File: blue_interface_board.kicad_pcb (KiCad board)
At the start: 4 copper layers, 70 x 70 mm, 123 parts, among them J1 arm connector, J2 USB_B_Micro, J3 ESTOP, J4 PWR, J5 Conn_ARM_JTAG_SWD_10, J6 logic-side RS485 debug/expans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, J7 FAN, J8 power-side RS485 debug/expans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, Q1 MMBT5401LT1G, Q2 Q_NMOS_GDS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

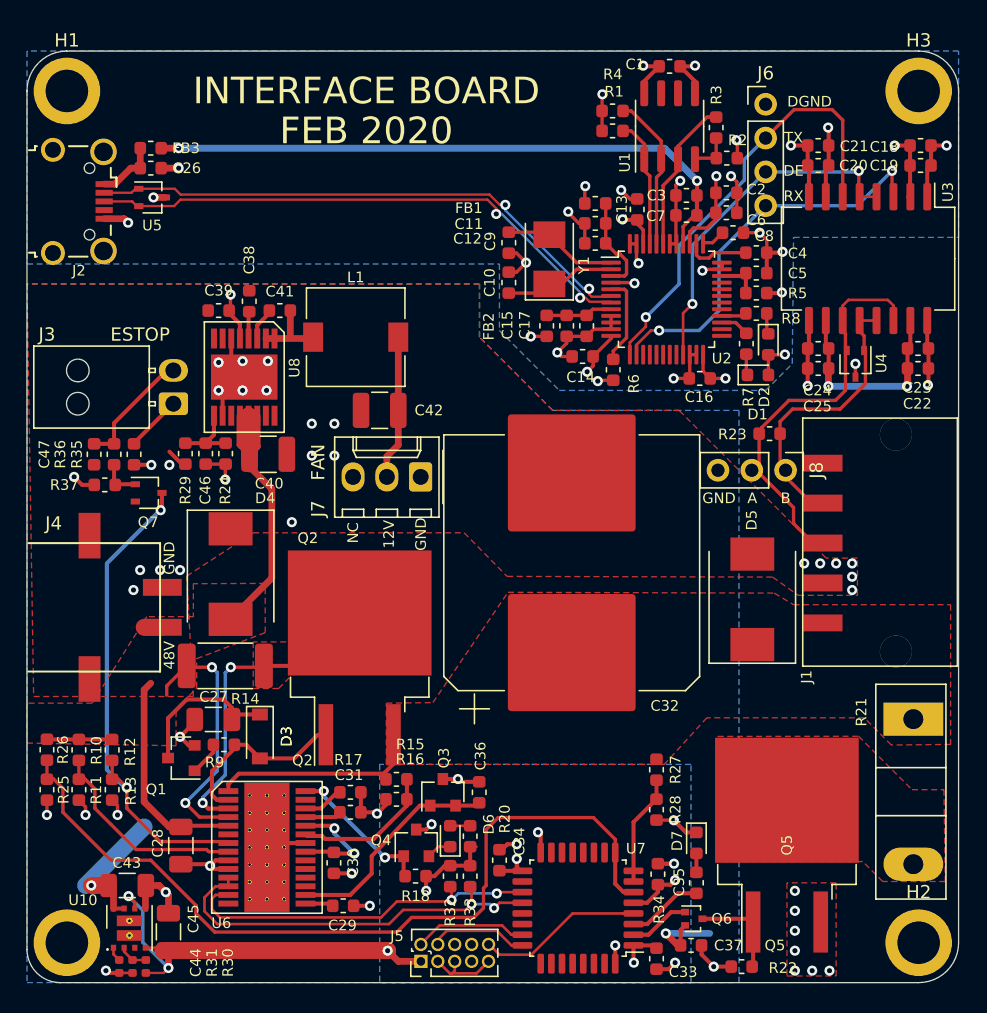
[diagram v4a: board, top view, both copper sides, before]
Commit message: recalculate lm5066 passives
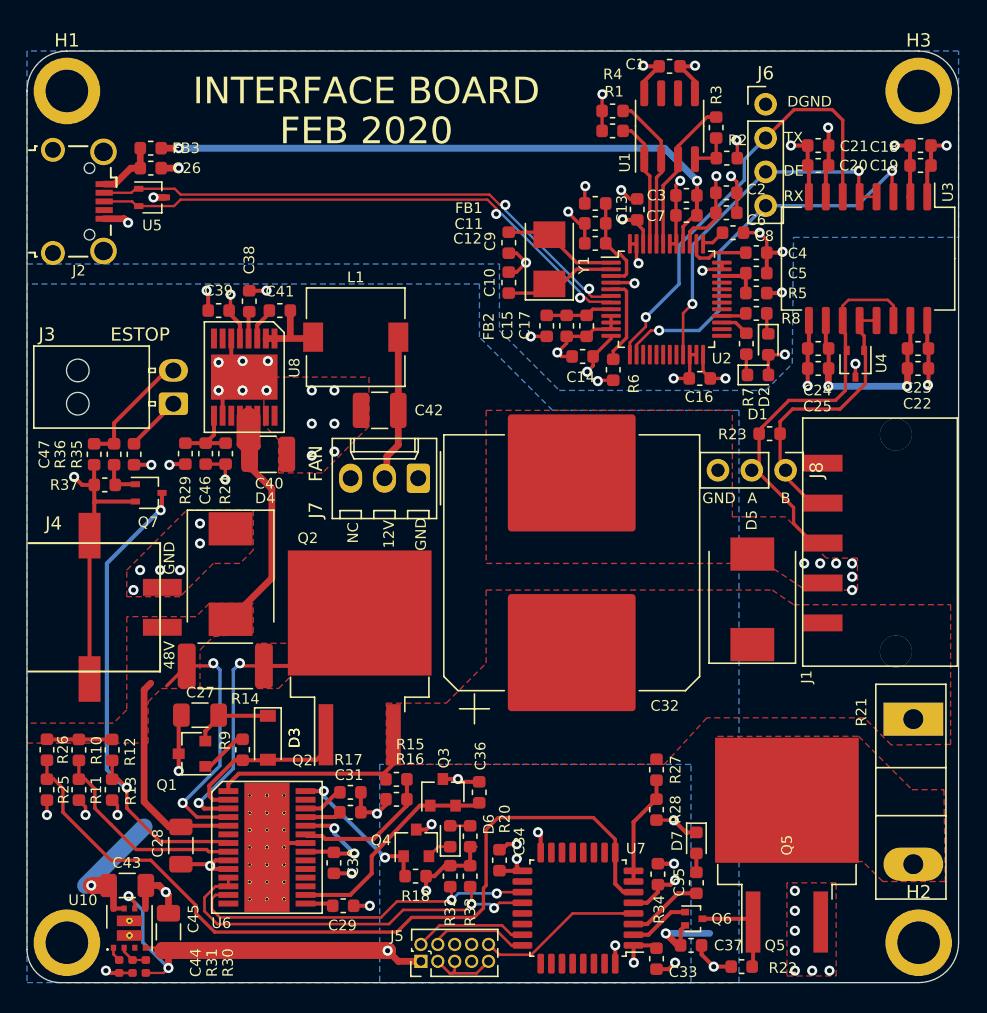
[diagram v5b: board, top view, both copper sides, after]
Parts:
- Q2: value Q_NMOS_GDS -> PSMN4R8-100BSEJ
- R11: value 6k65 -> 6k5
- R14: value 10m -> 15m
- R15: value 240k -> 140k
- R16: value 13.3k -> 21k
- R17: value 240k -> 21k
- moved R9 1.45 mm to (105.2, 111.5), turned to 90 degrees
- moved C27 1.05 mm to (102.0, 108.9)
- moved Q1 0.86 mm to (101.4, 111.8)
- moved D3 0.61 mm to (107.1, 110.6)
- moved J7 0.21 mm to (118.4, 91.1)
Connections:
- Q1 pad 2: GND -> Net-(C27-Pad1)
- Q1 pad 3: Net-(C27-Pad1) -> GND
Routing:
- net GND: track 73.3 -> 96.2 mm, vias 52 -> 57
- net Net-(C27-Pad1): track 11.8 -> 6.08 mm
- net /Power/VIN: track 66.7 -> 65.5 mm
- net Net-(Q1-Pad1): track 2.54 -> 3.64 mm

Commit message: fix Q3 pinout and chase a few part numbers
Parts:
- moved C36 0.63 mm to (122.3, 114.7), turned to -90 degrees
- moved Q3 0.45 mm to (119.8, 114.7)
- moved R15 0.36 mm to (116.4, 113.7)
- moved R16 0.36 mm to (116.4, 115.2)
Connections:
- Q3 pad 2: Net-(C36-Pad1) -> GND
- Q3 pad 3: GND -> Net-(C36-Pad1)
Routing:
- net Net-(R15-Pad1): track 11.1 -> 9.80 mm
- net Net-(C36-Pad1): track 16.7 -> 17.7 mm

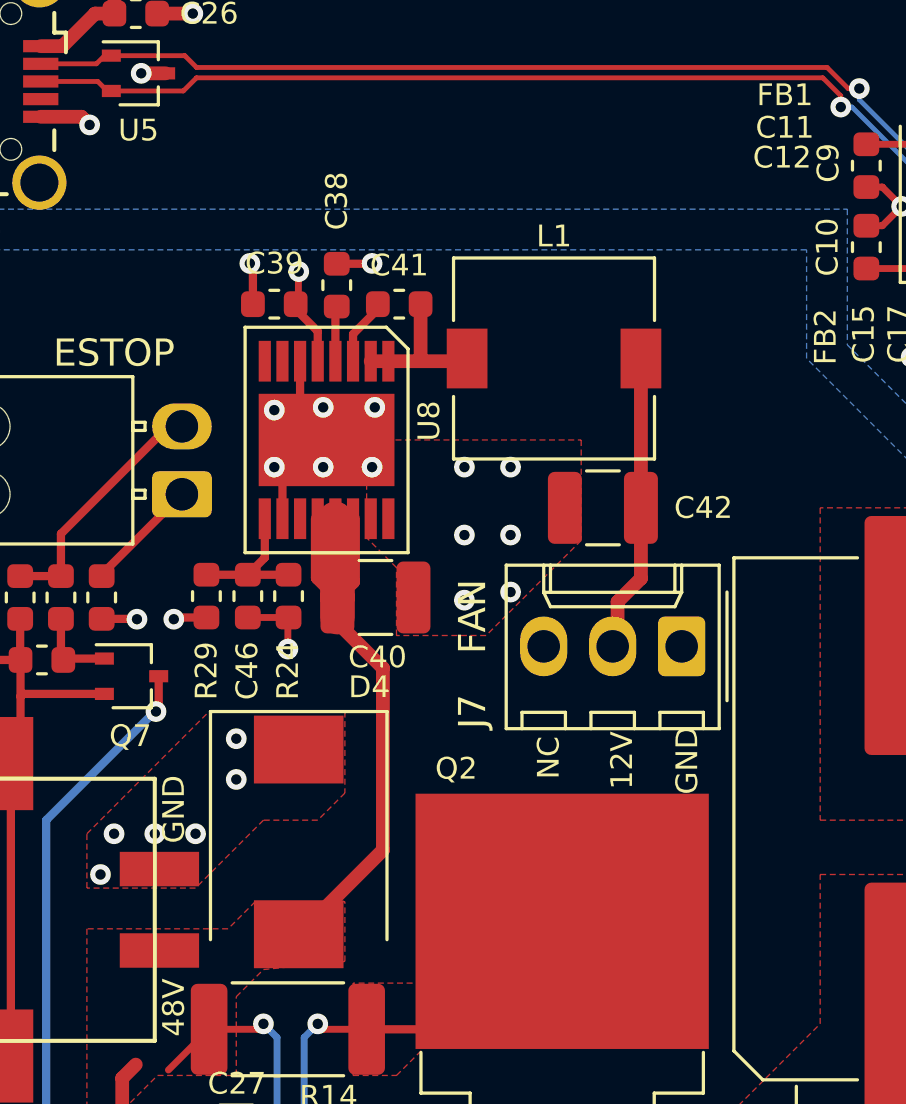
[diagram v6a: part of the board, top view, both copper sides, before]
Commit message: WIP 48v-12v dc/dc converter tweaks. need to restore to BLDC values
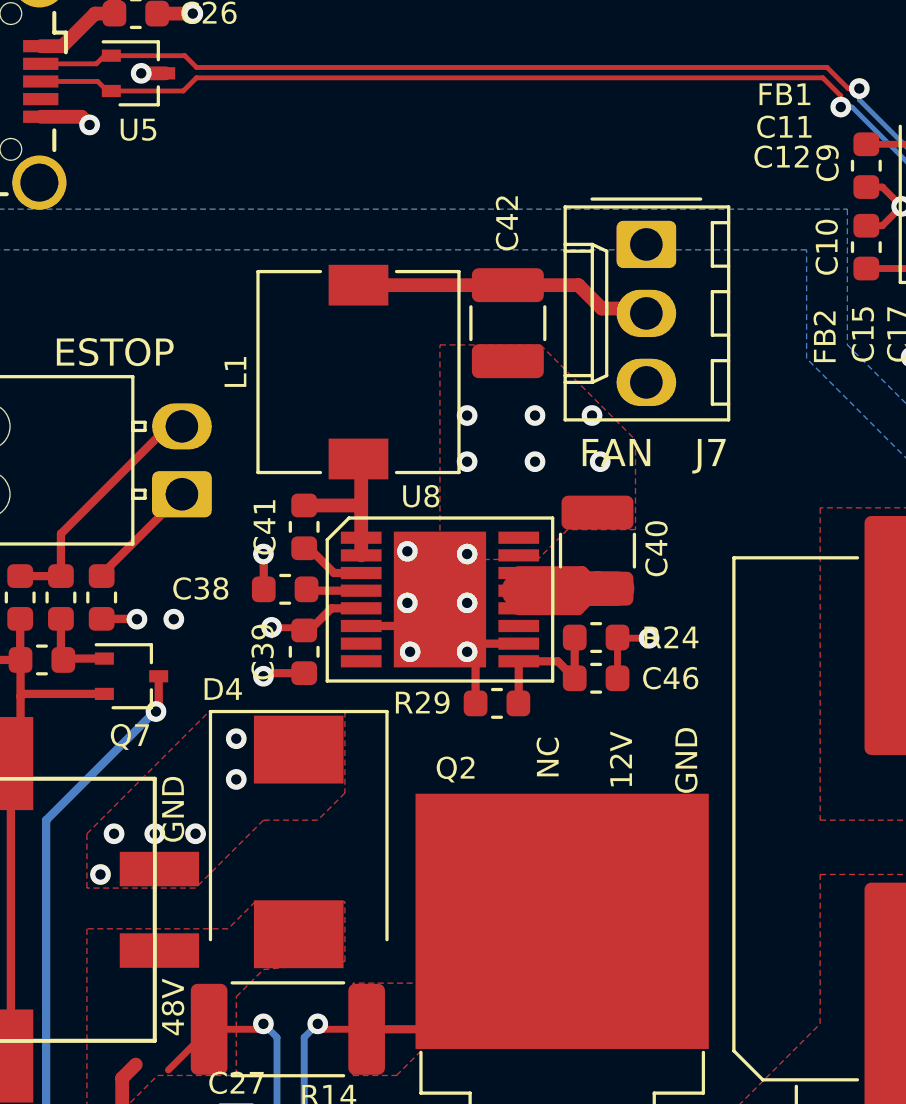
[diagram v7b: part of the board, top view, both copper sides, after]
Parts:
- moved J7 14.9 mm to (117.1, 76.3), turned to -90 degrees
- moved C46 13.2 mm to (115.2, 92.3), turned to 180 degrees
- moved C39 12.8 mm to (104.5, 91.3), turned to -90 degrees
- moved R24 11.4 mm to (115.2, 90.8), turned to 180 degrees
- moved R29 11.4 mm to (111.6, 93.2), turned to 180 degrees
- moved C38 11.4 mm to (103.8, 89.0), turned to 180 degrees
- moved C41 8.92 mm to (104.5, 86.7), turned to 90 degrees
- moved C40 8.36 mm to (115.3, 87.6), turned to 90 degrees
- moved C42 7.65 mm to (112.0, 79.2), turned to -90 degrees
- moved L1 7.22 mm to (106.5, 81.0), turned to 90 degrees
- moved U8 7.21 mm to (109.5, 89.4), turned to -90 degrees
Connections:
- C40 pad 1: /Power/VIN -> VOUT
- U8 pad 12: /Power/VIN -> VOUT
- U8 pad 13: /Power/VIN -> VOUT
- U8 pad 14: /Power/VIN -> VOUT
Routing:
- net /Power/VIN: track 65.5 -> 41.1 mm
- net VOUT: track 18.0 -> 28.9 mm
- net GND: track 96.6 -> 99.8 mm

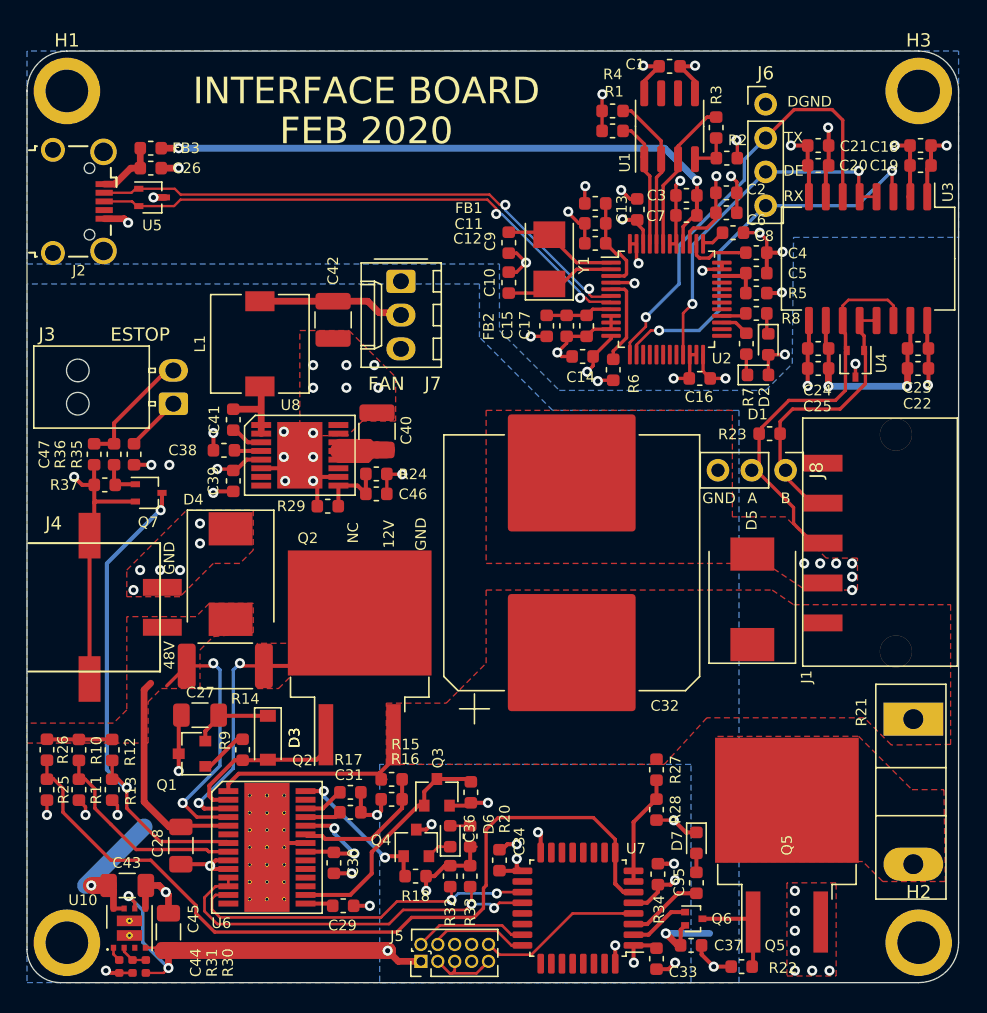
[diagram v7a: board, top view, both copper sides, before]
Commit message: add MCU reset cap, tweak dc-dc feedback divider
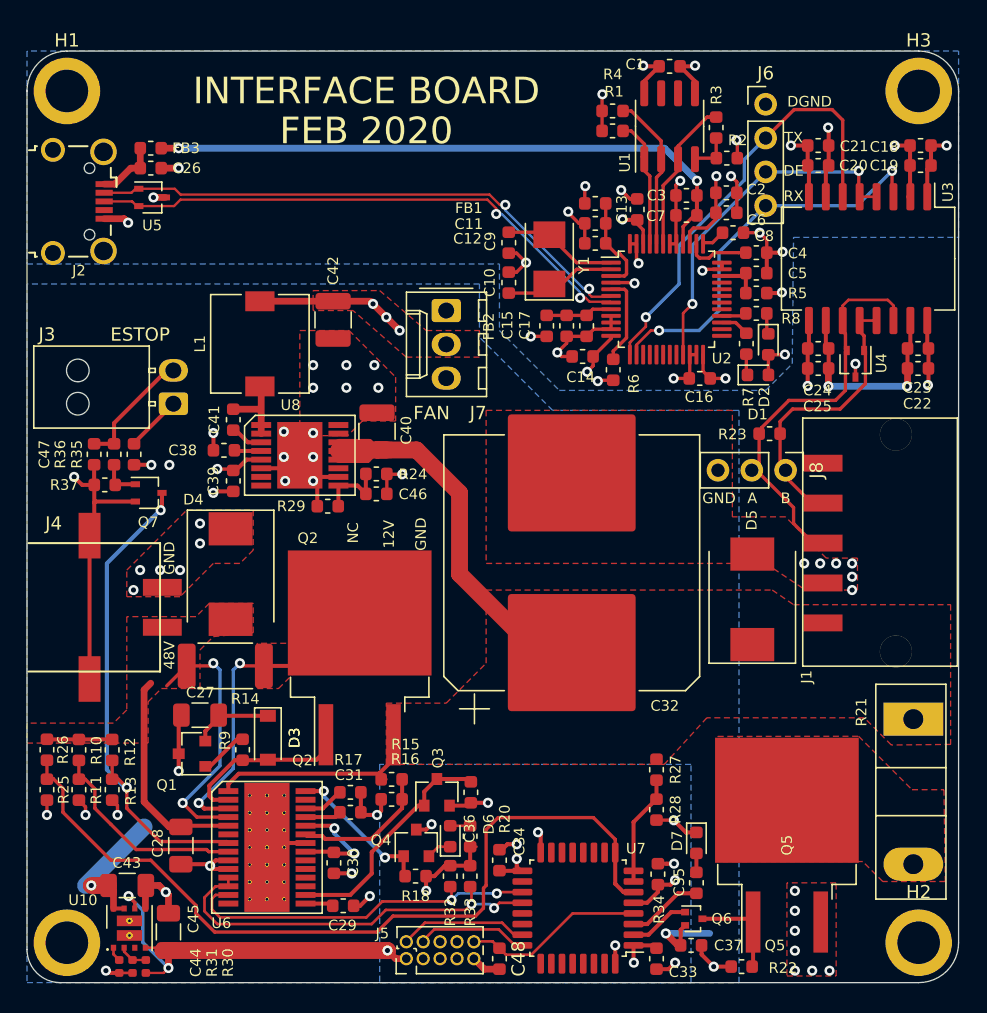
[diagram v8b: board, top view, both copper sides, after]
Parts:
- added C48: 100n, Capacitor_SMD:C_0603_1608Metric, F.Cu at (124.5, 127.2)
- C39: value 2u2 -> 1u
- moved J7 4.05 mm to (120.5, 78.5)
- moved J5 1.12 mm to (117.5, 127.2)
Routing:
- net VOUT: track 28.9 -> 53.4 mm
- net GND: track 99.8 -> 96.6 mm
- net /Power/SWDIO: track 8.52 -> 9.91 mm
- net /Power/nRST: track 12.5 -> 13.8 mm
- net /Power/SWDCLK: track 7.44 -> 8.63 mm
- net +3.3VP: track 49.6 -> 48.6 mm
- net +12V: track 35.2 -> 35.7 mm, vias 5 -> 8
- added copper zone on F.Cu, net +12V
